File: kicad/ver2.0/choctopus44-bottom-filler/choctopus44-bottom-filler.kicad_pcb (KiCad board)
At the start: 2 copper layers, 247.4 x 118.5 mm, 98 parts, among them SW1 SW_PUSH, SW10 SW_PUSH, SW11 SW_PUSH, SW12 SW_PUSH, SW13 SW_PUSH, SW14 SW_PUSH, SW15 SW_PUSH, SW16 SW_PUSH, SW17 SW_PUSH, SW18 SW_PUSH, SW19 SW_PUSH, SW2 SW_PUSH, SW20 SW_PUSH, SW21 SW_PUSH, SW22 SW_PUSH, SW23 SW_PUSH, SW24 SW_PUSH, SW25 SW_PUSH, SW26 SW_PUSH, SW27 SW_PUSH, SW28 SW_PUSH, SW29 SW_PUSH, SW3 SW_PUSH, SW30 SW_PUSH, SW31 SW_PUSH, SW32 SW_PUSH, SW33 SW_PUSH, SW34 SW_PUSH, SW35 SW_PUSH, SW36 SW_PUSH, SW37 SW_PUSH, SW38 SW_PUSH, SW39 SW_PUSH, SW4 SW_PUSH, SW40 SW_PUSH, SW41 SW_PUSH, SW42 SW_PUSH, SW43 SW_PUSH, SW44 SW_PUSH, SW45 Rotary_Encoder_Switch, SW5 SW_PUSH, SW6 SW_PUSH, SW7 SW_PUSH, SW8 SW_PUSH, SW9 SW_PUSH

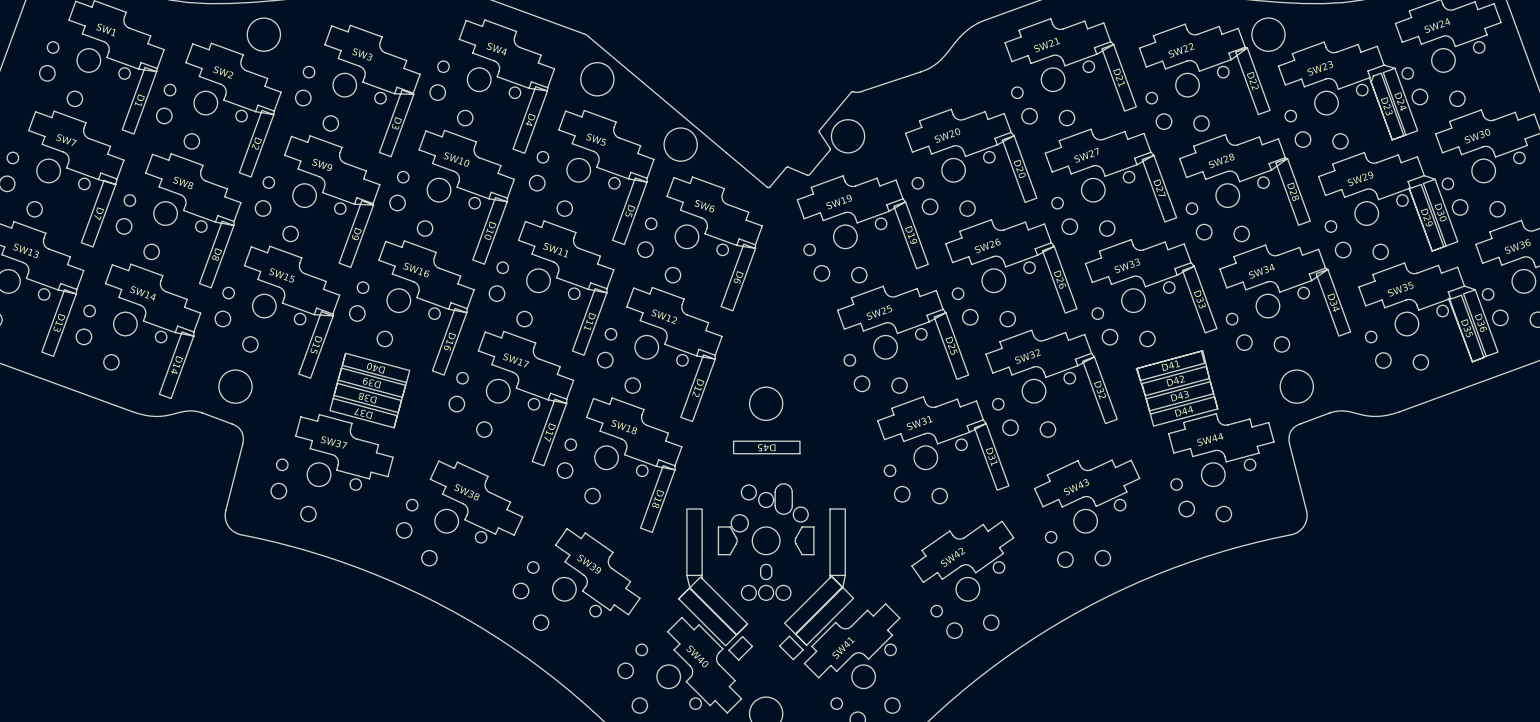
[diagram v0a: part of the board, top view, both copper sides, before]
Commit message: simplify filler foam files for faster laser cutting
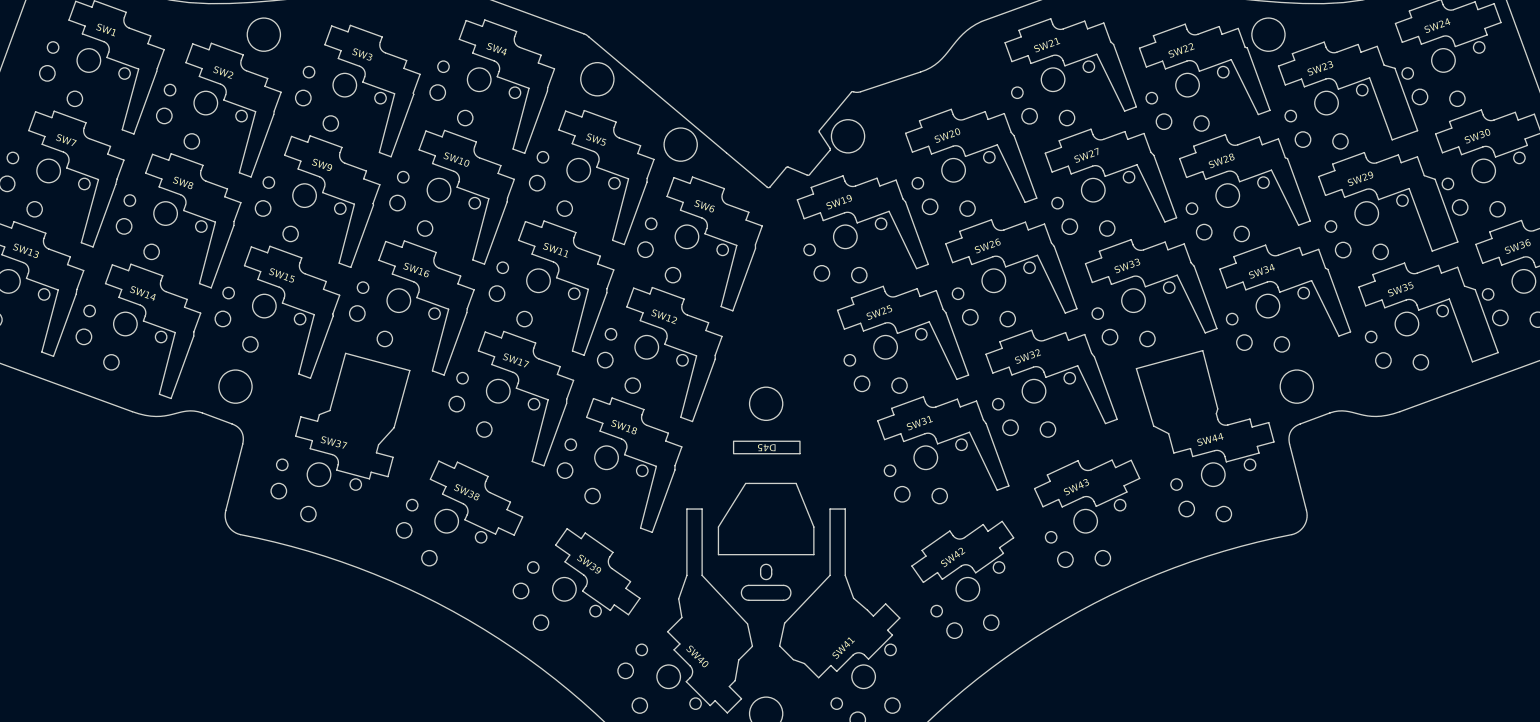
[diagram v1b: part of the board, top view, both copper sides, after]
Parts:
- removed C1, C2: C, custom-electronics:1206_hybrid-bottomfoam-cutout
- removed D1, D10, D11, D12, D13, D14, D15, D16, D17, D18, D19, D2, D20, D21, D22, D23, D24, D25, D26, D27, D28, D29, D3, D30, D31, D32, D33, D34, D35, D36, D37, D38, D39, D4, D40, D41, D42, D43, D44, D5, D6, D7, D8, D9: 1N4148W, custom-electronics:hybrid-diode-bottomfoam-cutout
- removed JP1, JP2: SolderJumper_2_Open, custom-electronics:jumper-bottomfoam-cutout
- removed R1, R2, R3, R4: R, custom-electronics:1206_hybrid-bottomfoam-cutout
- removed SW45: Rotary_Encoder_Switch, custom-electronics:ec11-bottomfoam-cutout
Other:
- outline, holes or cut-outs redrawn
